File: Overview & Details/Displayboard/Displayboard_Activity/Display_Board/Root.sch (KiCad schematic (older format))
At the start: 37 parts, among them J1 Micro_SD_Card_Det_MOD-Connect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, J2 Conn_01x20_Female, J4 Conn_01x20_Female, Q1 MMBT2222A-TP-dk_Transistors-B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, U1 MCP130T-300I_TT-dk_PMIC-Super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, U2 SN74LVC245AN-dk_Logic-Buffers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, U3 STMPE811QTR-Interface_Expansi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, U4 SN74LVC245AN-dk_Logic-Buffers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, U5 LP2988-3.3_SOIC8_VSSOP8

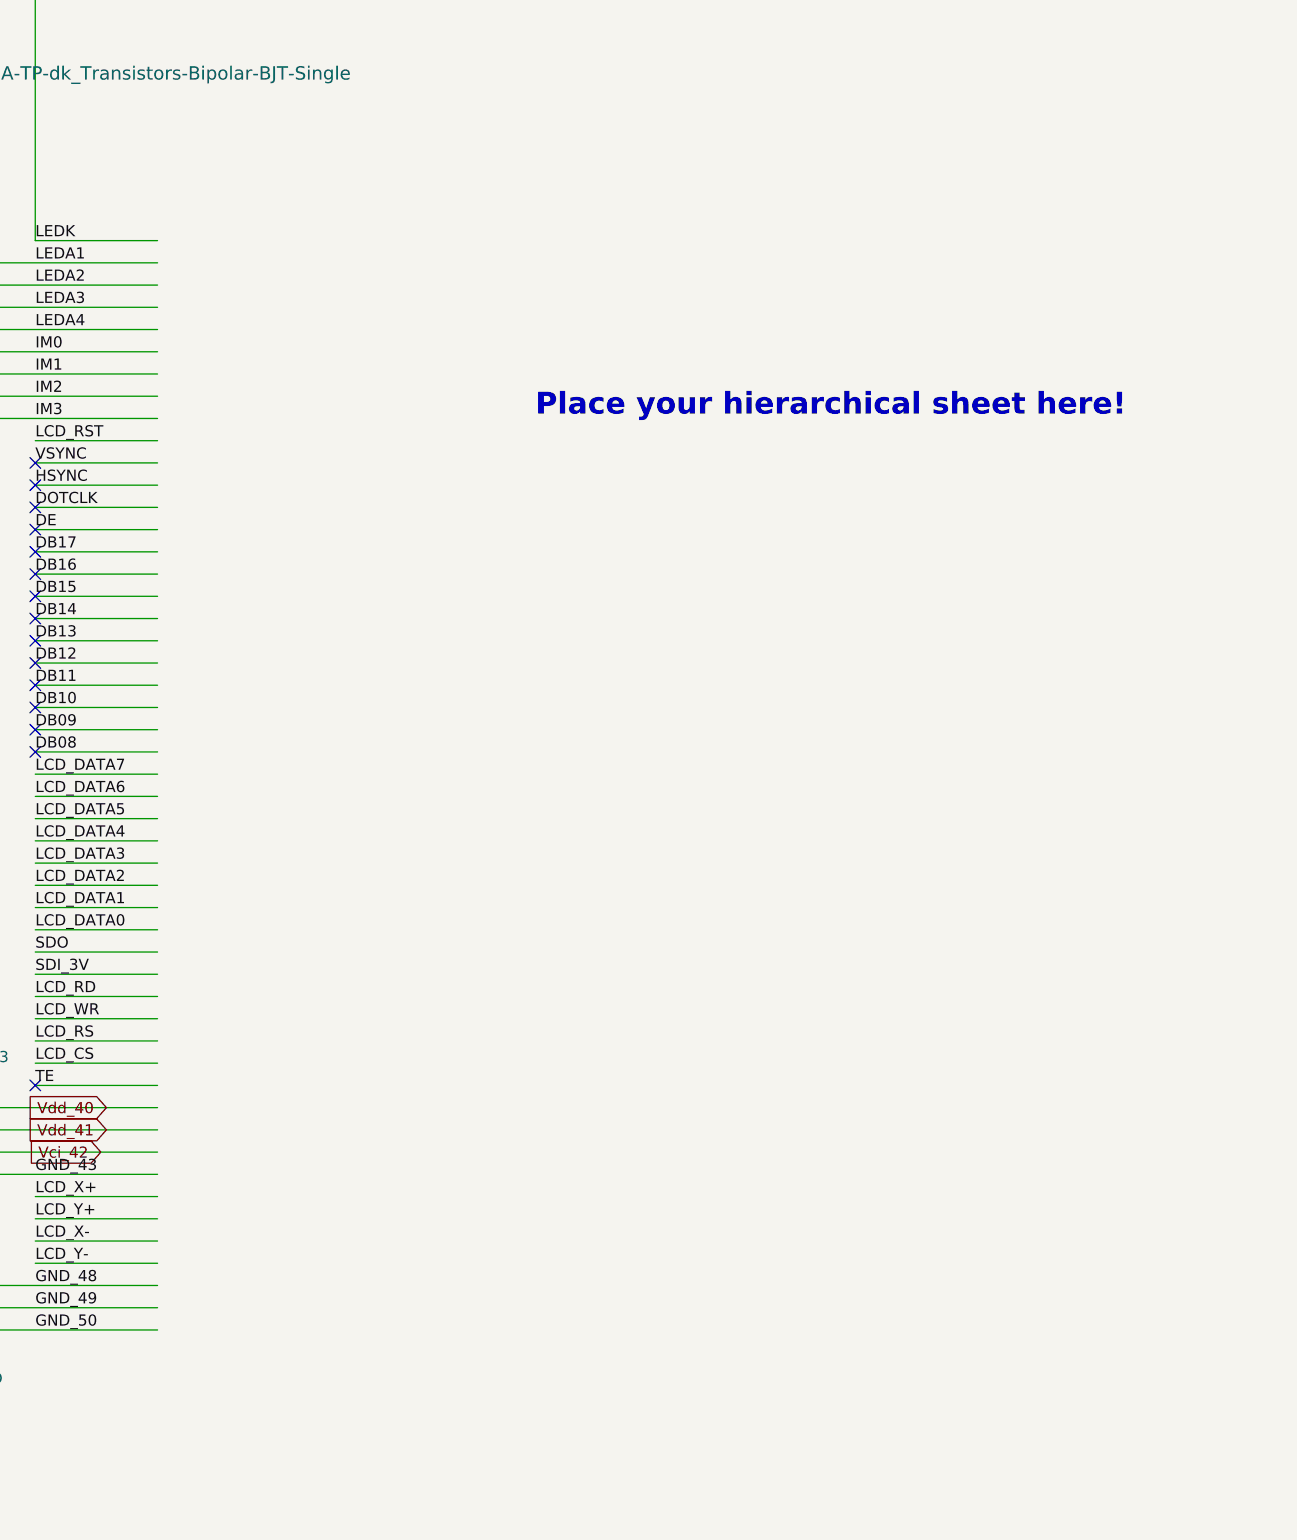
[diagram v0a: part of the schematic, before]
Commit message: Add hierarchical schematic
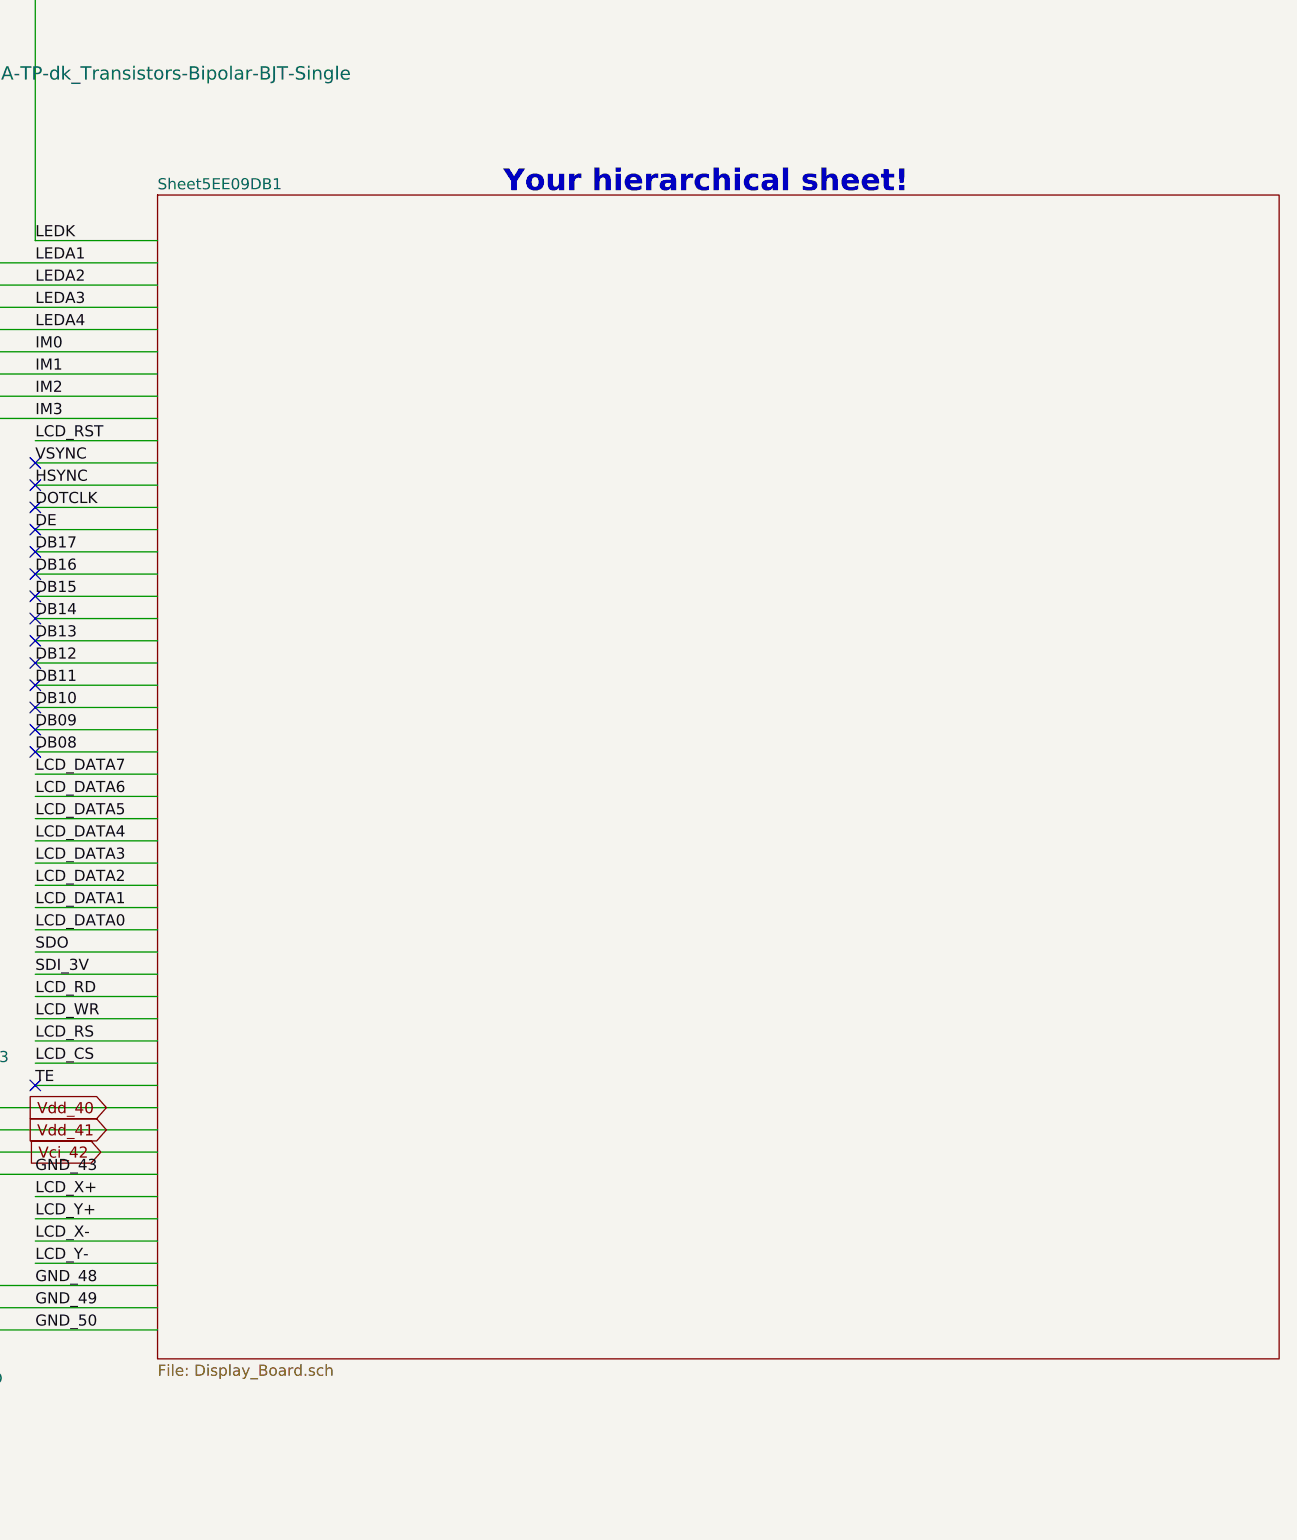
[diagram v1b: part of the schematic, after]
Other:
- note added: "Your hierarchical sheet!"
- note removed: "Place your hierarchical sheet here!"
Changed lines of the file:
@@
 NOTE: This schematic arrangement is meant to illustrate\n       the use of heirarchical sheets in a KiCad schematic.\n       It could also be done as a “flat” schematic.
 $Bitmap
-Pos 14050 5300
+Pos 13820 5300
 Scale 0.700000
 Data
@@
 	1    0    0    -1
 $EndComp
-Text Notes 12650 3750 0    98   ~ 20
-Place your hierarchical sheet here!
+Text Notes 12505 2745 0    98   ~ 20
+Your hierarchical sheet!
+$Sheet
+S 10950 2745 5045 5235
+U 5EE09DB2
+F0 "Sheet5EE09DB1" 50
+F1 "Display_Board.sch" 50
+$EndSheet
 $EndSCHEMATC
